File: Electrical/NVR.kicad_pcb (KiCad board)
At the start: 4 copper layers, 120 x 120 mm, 400 parts, among them IC1 RTL8125BG-CG, IC2 SiC437AED-T1-GE3, IC4 RTL8125BG-CG, J1 Bus_M.2_Socket_M, J10 87427-0442, J11 RJE3C1886401, J12 Conn_01x03_Pin, J13 SATA-A-PL-SMT-K, J14 SATA-A-PL-SMT-K, J15 Conn_01x03_Pin, J16 USB_C_Receptacle_USB2.0, J17 53261-0271, J19 SATA-A-PL-SMT-K, J2 RJE3C1886401, J20 SATA-A-PL-SMT-K, J21 SATA-A-PL-SMT-K, J22 SATA-A-PL-SMT-K, J3 HDMI_A, J4 USB3_A_Stacked, J5 USB_A_Stacked, J6 Bus_M.2_Socket_E, J7 87427-0442, J8 87427-0442, J9 87427-0442, M1 Fan_4pin, M2 Fan_4pin, Q1 2N7002, Q10 2N7002, Q2 2SK3018, Q3 2SK3018, Q4 2SK3018, Q8 2N7002, Q9 2N7002, SW1 SW_Push, U1 TPAZ1023-04F, U11 W25Q128JVSIQ, U13 HT7533, U14 CH224Q_C46061833, U15 SY8253ADC, U16 SY8253ADC, U2 TPAZ1023-04F, U3 ULC0524P, U4 ULC0524P, U5 ULC0524P, U6 SY8253ADC, U7 SY8253ADC, U79 W25Q128JVSIQ, U8 ASM1166, Y1 25MHz, Y2 25MHz, Y4 25MHz

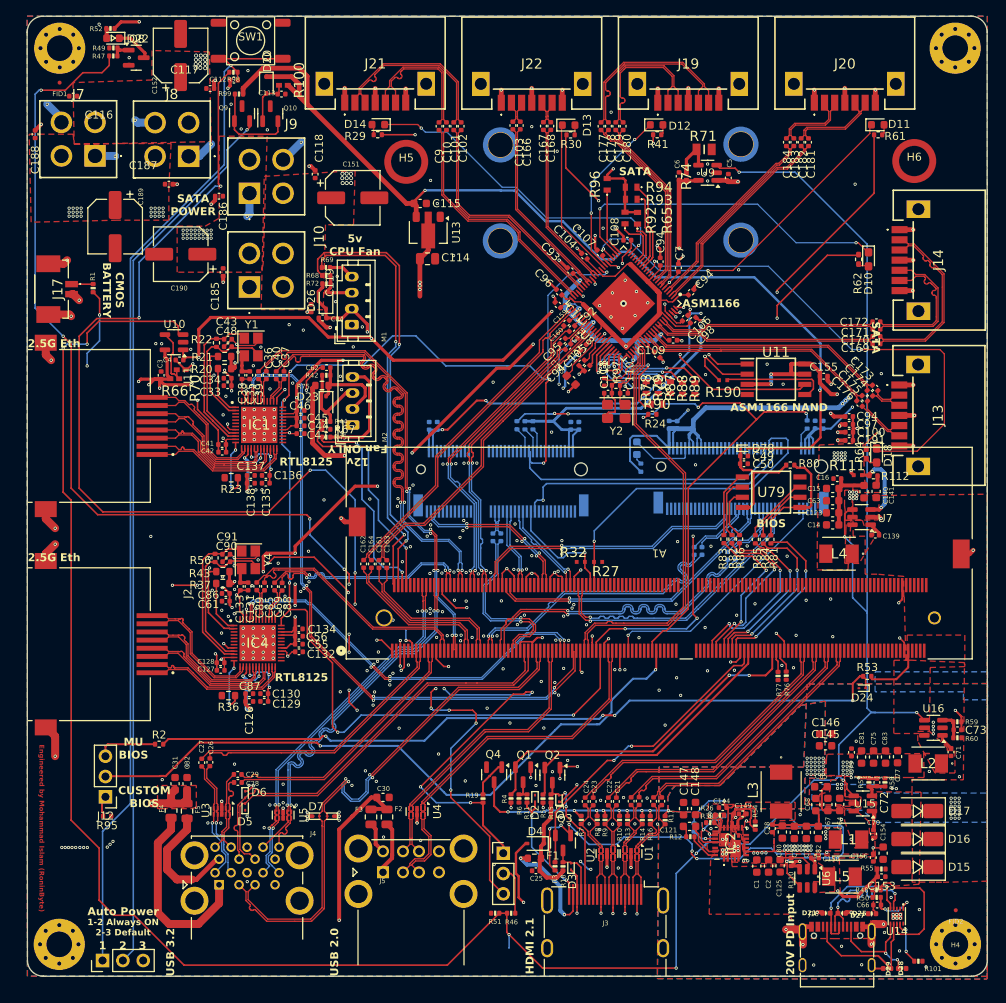
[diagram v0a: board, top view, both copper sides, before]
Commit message: changed ethernet port
changed to one that has built in magnetics
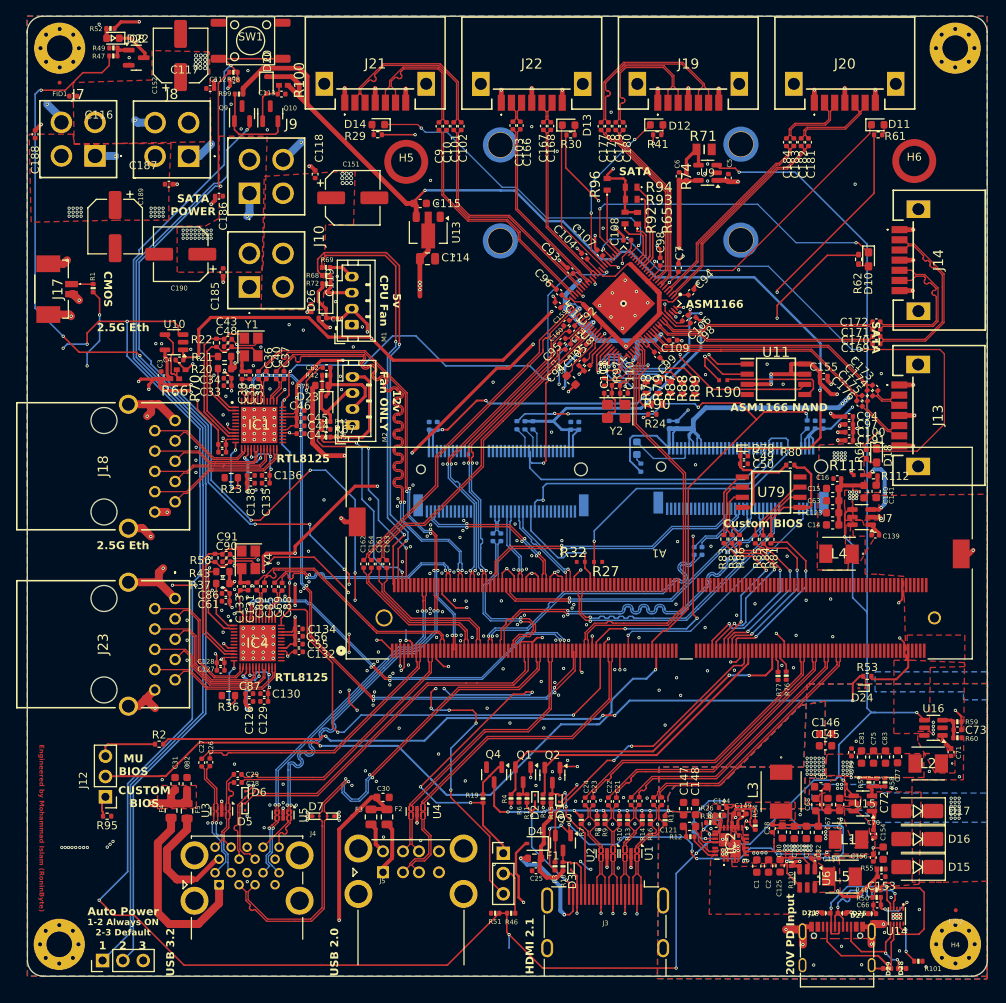
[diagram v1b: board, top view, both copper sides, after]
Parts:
- removed J11, J2: RJE3C1886401, amp eth:AMPHENOL_RJE3C1886401
- added J18: HFJ11-2G48ERL, new eth:HFJ112G48ERL, F.Cu at (236.5, 198.5)
- added J23: HFJ11-2G48ERL, new eth:HFJ112G48ERL, F.Cu at (236.5, 220.8)
- renumbered C94 to C98
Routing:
- net /LattePanda Module/~{PWR_SW}: track 124.2 -> 105.5 mm
- net GND: track 288.8 -> 304.4 mm, vias 409 -> 414
- net /PSU/PWR_EN: track 354.3 -> 364.8 mm, vias 11 -> 13
- net Net-(J15-Pin_2): track 111.5 -> 119.1 mm
- net Net-(J15-Pin_1): track 130.6 -> 137.8 mm
- net /~{PWR_LED}/~{PSON}: track 177.5 -> 170.8 mm, vias 11 -> 13
- net /Gigabit Ethernet/MDI0-: track 17.4 -> 11.4 mm
- net /Gigabit Ethernet/MDI1-: track 18.3 -> 12.9 mm
- net /Gigabit Ethernet/MDI2-: track 18.8 -> 14.1 mm
- net /Gigabit Ethernet/MDI0+: track 17.4 -> 13.2 mm
- net /Gigabit Ethernet/MDI1+: track 18.3 -> 14.6 mm
- net /Gigabit Ethernet/MDI2+: track 18.8 -> 15.8 mm
- net +0V9: track 193.5 -> 196.4 mm
- net /Gigabit Ethernet/MDI_3-: track 18.4 -> 15.7 mm
- net /Gigabit Ethernet/MDI3-: track 18.6 -> 16.2 mm
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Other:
- board text added: "CMOS"
- board text added: "Custom BIOS"
- board text removed: "BIOS"
- board text removed: "CMOS BATTERY"
